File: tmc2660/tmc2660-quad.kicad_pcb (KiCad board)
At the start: 4 copper layers, 26.7 x 31.1 mm, 17 parts, among them J1 0R, P3 Motor, U1 TMC2660

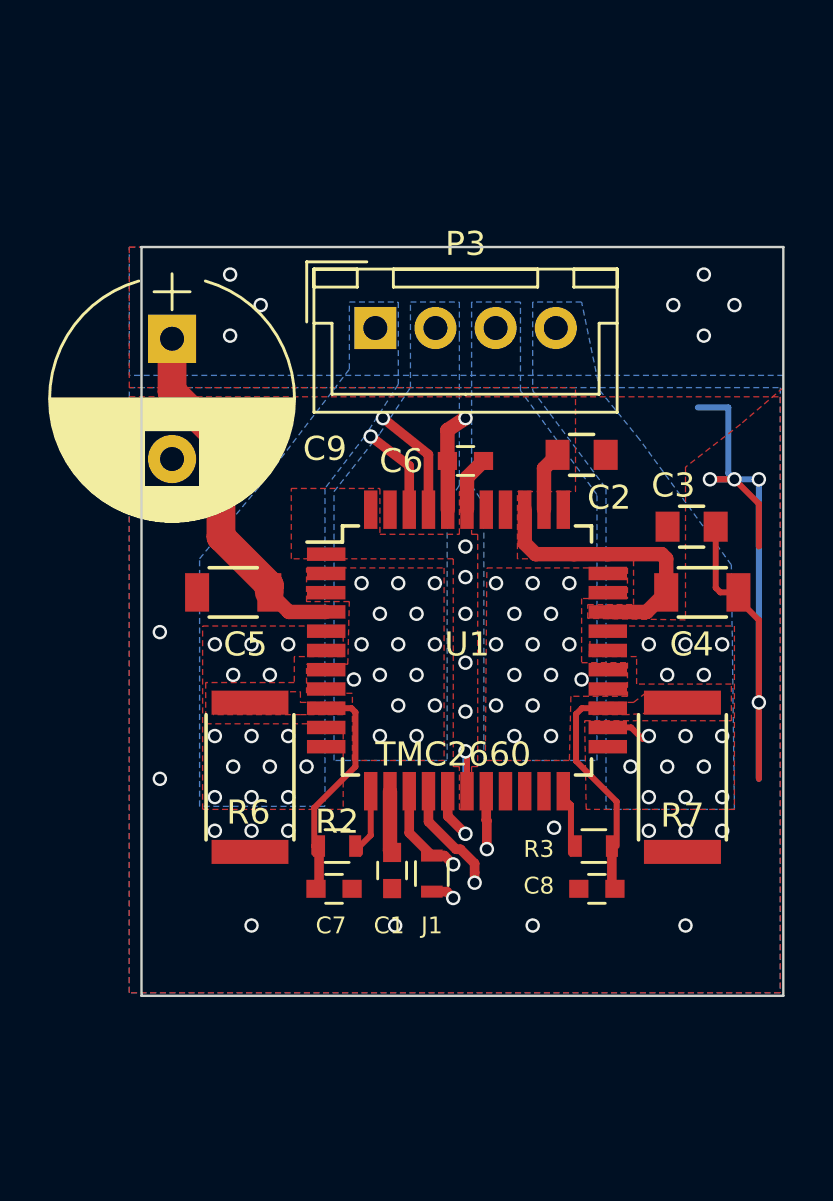
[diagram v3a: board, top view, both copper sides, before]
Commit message: Add mounting holes; trim sizes to 'round' values.
o Size of board is 25mmx40mm
o Distance M2.5 mounting holes: 35mm
o Width needs to be a 'round' number so that replicated
  drivers have properly distanted mounting holes.
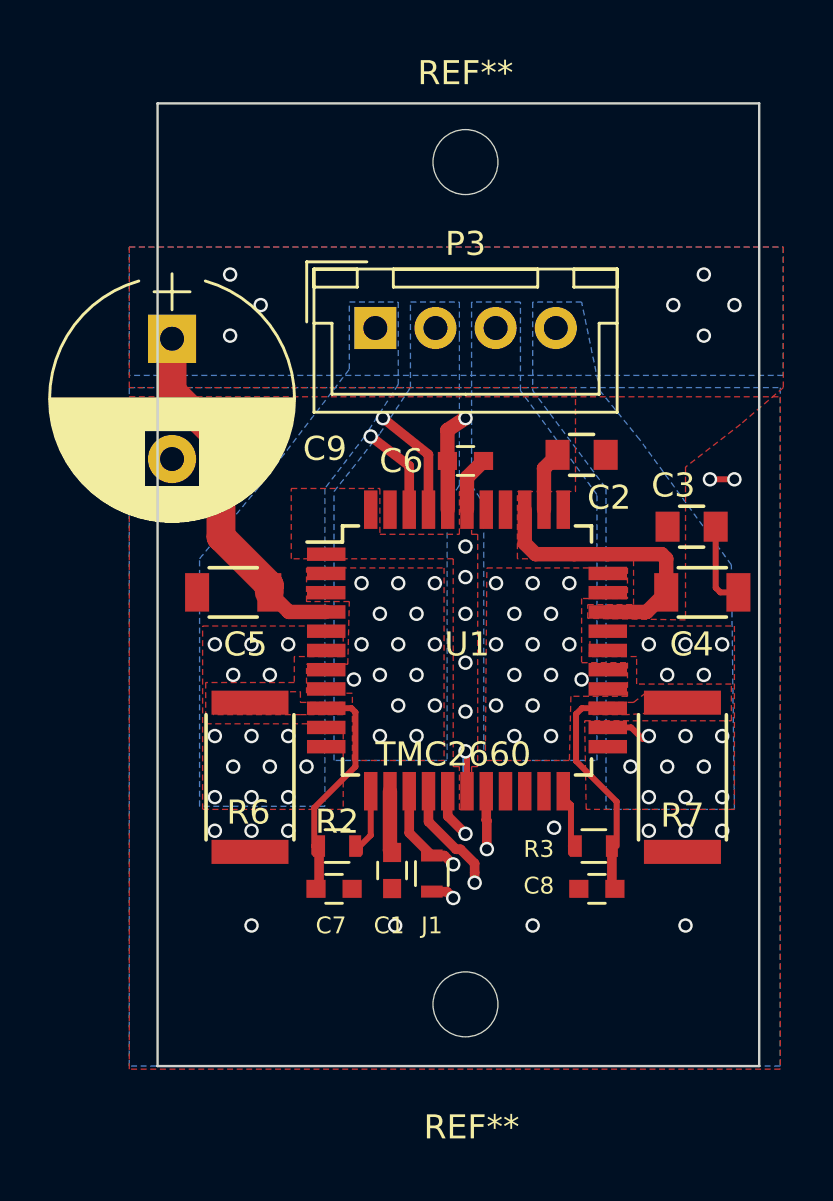
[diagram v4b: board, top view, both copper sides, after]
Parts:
- added REF**: M2.5, Mounting_Holes:MountingHole_2.7mm_M2.5, F.Cu at (129.8, 34.1)
- added REF**: M2.5, Mounting_Holes:MountingHole_2.7mm_M2.5, F.Cu at (129.8, 69.1)
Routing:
- net GND: track 39.7 -> 9.82 mm, vias 29 -> 23
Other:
- board size 26.7 x 31.1 mm -> 25 x 40 mm
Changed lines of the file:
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@@
   (thickness 1.6)
   (drawings 6)
-  (tracks 217)
+  (tracks 199)
   (zones 0)
-  (modules 17)
+  (modules 19)
   (nets 23)
 )
@@
 )
 (setup
-  (last_trace_width 0.4)
+  (last_trace_width 0.25)
   (user_trace_width 0.4)
   (user_trace_width 0.6)
@@
   (mod_text_size 1 1)
   (mod_text_width 0.15)
-  (pad_size 1 3.2)
-  (pad_drill 0)
+  (pad_size 2.7 2.7)
+  (pad_drill 2.7)
   (pad_to_mask_clearance 0)
   (aux_axis_origin 0 0)
@@
   (add_net VMot)
 )
+  (module Mounting_Holes:MountingHole_2.7mm_M2.5 (layer F.Cu)
+    (at 129.794 34.062)
+    (descr "Mounting Hole 2.7mm, no annular, M2.5")
+    (tags "mounting hole 2.7mm no annular m2.5")
+    (attr virtual)
+    (fp_text reference REF** (at 0 -3.7) (layer F.SilkS)
+      (effects (font (size 1 1) (thickness 0.15)))
+    )
+    (fp_text value M2.5 (at 4.064 -4.318) (layer F.Fab)
+      (effects (font (size 1 1) (thickness 0.15)))
+    )
+    (fp_circle (center 0 0) (end 2.95 0) (layer F.CrtYd) (width 0.05))
+    (fp_circle (center 0 0) (end 2.7 0) (layer Cmts.User) (width 0.15))
+    (fp_text user %R (at 0.3 0) (layer F.Fab)
+      (effects (font (size 1 1) (thickness 0.15)))
+    )
+    (pad "" np_thru_hole circle (at 0 0) (size 2.7 2.7) (drill 2.7) (layers *.Cu *.Mask)
+      (clearance 2))
+  )
+  (module Mounting_Holes:MountingHole_2.7mm_M2.5 (layer F.Cu)
+    (at 129.794 69.062)
+    (descr "Mounting Hole 2.7mm, no annular, M2.5")
+    (tags "mounting hole 2.7mm no annular m2.5")
+    (attr virtual)
+    (fp_text reference REF** (at 0.254 5.106) (layer F.SilkS)
+      (effects (font (size 1 1) (thickness 0.15)))
+    )
+    (fp_text value M2.5 (at 0 3.7) (layer F.Fab)
+      (effects (font (size 1 1) (thickness 0.15)))
+    )
+    (fp_circle (center 0 0) (end 2.95 0) (layer F.CrtYd) (width 0.05))
+    (fp_circle (center 0 0) (end 2.7 0) (layer Cmts.User) (width 0.15))
+    (fp_text user %R (at 0.3 0) (layer F.Fab)
+      (effects (font (size 1 1) (thickness 0.15)))
+    )
+    (pad "" np_thru_hole circle (at 0 0) (size 2.7 2.7) (drill 2.7) (layers *.Cu *.Mask)
+      (clearance 0.5))
+  )
   (module Resistors_SMD:R_0603 (layer F.Cu)
     (at 128.397 63.627 90)
@@
     (effects (font (size 1.2 1.2) (thickness 0.25)) (justify right mirror))
   )
-  (gr_line (start 116.332 68.707) (end 116.332 37.592) (layer Edge.Cuts) (width 0.1))
-  (gr_line (start 143.002 68.707) (end 116.332 68.707) (layer Edge.Cuts) (width 0.1))
-  (gr_line (start 143.002 37.592) (end 143.002 68.707) (layer Edge.Cuts) (width 0.1))
-  (gr_line (start 116.332 37.592) (end 143.002 37.592) (layer Edge.Cuts) (width 0.1))
+  (gr_line (start 117 71.628) (end 117 31.623) (layer Edge.Cuts) (width 0.1))
+  (gr_line (start 142 71.628) (end 117 71.628) (layer Edge.Cuts) (width 0.1))
+  (gr_line (start 142 31.623) (end 142 71.628) (layer Edge.Cuts) (width 0.1))
+  (gr_line (start 117 31.623) (end 142 31.623) (layer Edge.Cuts) (width 0.1))
   (via (at 133.477 61.722) (size 0.6) (drill 0.4) (layers F.Cu B.Cu) (net 1))
   (via (at 138.938 65.786) (size 0.6) (drill 0.4) (layers F.Cu B.Cu) (net 1))
@@
   (segment (start 129.8575 48.506) (end 129.8575 47.1685) (width 0.6) (layer F.Cu) (net 1))
   (segment (start 129.8575 47.1685) (end 130.544 46.482) (width 0.6) (layer F.Cu) (net 1))
-  (via (at 116.967 44.704) (size 0.6) (drill 0.4) (layers F.Cu B.Cu) (net 1))
-  (via (at 116.967 48.514) (size 0.6) (drill 0.4) (layers F.Cu B.Cu) (net 1))
-  (via (at 118.237 48.514) (size 0.6) (drill 0.4) (layers F.Cu B.Cu) (net 1))
+  (via (at 117.602 48.387) (size 0.6) (drill 0.4) (layers F.Cu B.Cu) (net 1))
   (via (at 121.285 45.339) (size 0.6) (drill 0.4) (layers F.Cu B.Cu) (net 1))
   (via (at 122.047 44.45) (size 0.6) (drill 0.4) (layers F.Cu B.Cu) (net 1))
   (via (at 120.523 44.45) (size 0.6) (drill 0.4) (layers F.Cu B.Cu) (net 1))
-  (via (at 117.094 53.594) (size 0.6) (drill 0.4) (layers F.Cu B.Cu) (net 1))
   (via (at 140.462 61.849) (size 0.6) (drill 0.4) (layers F.Cu B.Cu) (net 1))
   (via (at 138.938 61.849) (size 0.6) (drill 0.4) (layers F.Cu B.Cu) (net 1))
@@
   (via (at 129.794 54.864) (size 0.6) (drill 0.4) (layers F.Cu B.Cu) (net 1))
   (via (at 129.794 56.896) (size 0.6) (drill 0.4) (layers F.Cu B.Cu) (net 1))
-  (via (at 117.094 59.69) (size 0.6) (drill 0.4) (layers F.Cu B.Cu) (net 1))
   (segment (start 126.6575 60.206) (end 126.6575 62.6615) (width 0.6) (layer F.Cu) (net 2))
   (segment (start 126.6575 62.6615) (end 126.746 62.75) (width 0.6) (layer F.Cu) (net 2))
@@
   (segment (start 133.62 46.228) (end 133.0575 46.7905) (width 0.6) (layer F.Cu) (net 4))
   (segment (start 133.0575 46.7905) (end 133.0575 48.506) (width 0.6) (layer F.Cu) (net 4))
-  (segment (start 140.716 44.2595) (end 139.45 44.2595) (width 0.25) (layer B.Cu) (net 1))
-  (segment (start 141.986 55.626) (end 141.986 59.69) (width 0.25) (layer B.Cu) (net 1))
-  (segment (start 141.986 47.244) (end 141.986 50.038) (width 0.25) (layer B.Cu) (net 1))
-  (segment (start 139.954 47.244) (end 141.986 47.244) (width 0.25) (layer B.Cu) (net 1))
-  (via (at 141.986 47.244) (size 0.6) (drill 0.4) (layers F.Cu B.Cu) (net 1))
   (segment (start 140.97 47.244) (end 139.954 47.244) (width 0.25) (layer F.Cu) (net 1))
   (via (at 139.954 47.244) (size 0.6) (drill 0.4) (layers F.Cu B.Cu) (net 1))
-  (segment (start 141.986 53.0925) (end 141.986 55.626) (width 0.25) (layer F.Cu) (net 1))
-  (segment (start 141.986 55.626) (end 141.986 59.69) (width 0.25) (layer F.Cu) (net 1))
-  (via (at 141.986 56.515) (size 0.6) (drill 0.4) (layers F.Cu B.Cu) (net 1))
-  (segment (start 141.986 50.038) (end 141.986 55.626) (width 0.25) (layer B.Cu) (net 1))
-  (segment (start 140.97 47.244) (end 141.986 48.26) (width 0.25) (layer F.Cu) (net 1))
-  (segment (start 141.986 48.26) (end 141.986 50.038) (width 0.25) (layer F.Cu) (net 1))
-  (segment (start 140.716 44.2595) (end 140.716 46.99) (width 0.25) (layer B.Cu) (net 1))
-  (segment (start 140.716 46.99) (end 140.97 47.244) (width 0.25) (layer B.Cu) (net 1))
   (via (at 140.97 47.244) (size 0.6) (drill 0.4) (layers F.Cu B.Cu) (net 1))
   (segment (start 141.1365 51.943) (end 141.1365 52.243) (width 0.25) (layer F.Cu) (net 1) (status 30))
-  (segment (start 141.1365 52.243) (end 141.986 53.0925) (width 0.25) (layer F.Cu) (net 1) (status 10))
   (segment (start 140.192 49.2125) (end 140.192 51.7485) (width 0.25) (layer F.Cu) (net 1) (status 10))
   (segment (start 140.192 51.7485) (end 140.3865 51.943) (width 0.25) (layer F.Cu) (net 1))
@@
     (polygon
       (pts
-        (xy 115.824 43.815) (xy 142.875 43.815) (xy 142.875 68.58) (xy 115.824 68.58)
+        (xy 115.824 43.815) (xy 142.875 43.815) (xy 142.875 71.755) (xy 115.824 71.755)
       )
     )
@@
     (polygon
       (pts
-        (xy 115.824 43.434) (xy 142.875 43.434) (xy 142.875 68.58) (xy 115.824 68.58)
+        (xy 115.824 43.434) (xy 142.875 43.434) (xy 142.875 71.628) (xy 115.824 71.628)
       )
     )
@@
     (polygon
       (pts
-        (xy 115.824 43.688) (xy 143.002 43.688) (xy 143.002 68.58) (xy 115.824 68.58)
+        (xy 115.824 43.688) (xy 143.002 43.688) (xy 143.002 71.628) (xy 115.824 71.628)
       )
     )
@@
     (min_thickness 0.254)
     (keepout (tracks allowed) (vias allowed) (copperpour not_allowed))
-    (fill (arc_segments 16) (thermal_gap 0.508) (thermal_bridge_width 0.508))
+    (fill yes (arc_segments 16) (thermal_gap 0.508) (thermal_bridge_width 0.508))
     (polygon
       (pts
@@
     (min_thickness 0.254)
     (keepout (tracks not_allowed) (vias allowed) (copperpour allowed))
-    (fill (arc_segments 16) (thermal_gap 0.508) (thermal_bridge_width 0.508))
+    (fill yes (arc_segments 16) (thermal_gap 0.508) (thermal_bridge_width 0.508))
     (polygon
       (pts
@@
     (min_thickness 0.254)
     (keepout (tracks not_allowed) (vias allowed) (copperpour allowed))
-    (fill (arc_segments 16) (thermal_gap 0.508) (thermal_bridge_width 0.508))
+    (fill yes (arc_segments 16) (thermal_gap 0.508) (thermal_bridge_width 0.508))
     (polygon
       (pts
@@
     (min_thickness 0.254)
     (keepout (tracks not_allowed) (vias allowed) (copperpour allowed))
-    (fill (arc_segments 16) (thermal_gap 0.508) (thermal_bridge_width 0.508))
+    (fill yes (arc_segments 16) (thermal_gap 0.508) (thermal_bridge_width 0.508))
     (polygon
       (pts
@@
     (polygon
       (pts
-        (xy 115.824 61.341) (xy 143.002 61.341) (xy 143.002 68.707) (xy 115.824 68.707)
+        (xy 115.824 61.341) (xy 143.002 61.341) (xy 143.002 71.755) (xy 115.824 71.755)
       )
     )
@@
       )
     )
+  )
+  (zone (net 0) (net_name "") (layers F&B.Cu) (hatch edge 0.508)
+    (connect_pads (clearance 0.5))
+    (min_thickness 0.254)
+    (keepout (tracks not_allowed) (vias not_allowed) (copperpour not_allowed))
+    (fill yes (arc_segments 16) (thermal_gap 0.508) (thermal_bridge_width 0.508))
+    (polygon
+      (pts
+        (xy 126.746 70.358) (xy 128.524 72.136) (xy 131.064 72.136) (xy 132.842 70.358) (xy 132.842 67.691)
+        (xy 131.064 66.04) (xy 128.397 66.04) (xy 126.746 67.691)
+      )
+    )
